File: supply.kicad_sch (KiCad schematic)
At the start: 70 parts, among them J3 Molex_Nano-Fit_1x2_SMD_105430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, Q2 SSM3J332R, Q3 SSM3J332R, Q4 BCM857BS-7-F, Q5 BCM857BS-7-F, Q6 SSM3J332R, Q7 PJE138K, Q8 PJE138K, Q9 SSM3J332R, U1 TPS56C230, U2 TPS56C230

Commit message: [#53804] Clean SD&NVMe sch; Change NVMe to x4; Update 3V3 power sch
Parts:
- removed C11: C_1u_0402, antmicro-footprints:C_0402_1005Metric, symbol antmicroCapacitors0402:C_1u_0402
- removed C13, C9: C_100n_0402, antmicro-footprints:C_0402_1005Metric, symbol antmicroCapacitors0402:C_100n_0402
- removed C14, C16, C18, C20: C_22u_16V_0603, antmicro-footprints:C_0603_1608Metric, symbol antmicroCapacitors0603:C_22u_16V_0603
- removed C5, C7: C_22u_25V_0805, antmicro-footprints:C_0805_2012Metric, symbol antmicroCapacitorsmisc:C_22u_25V_0805
- removed D7: ESD9X5.0ST5G, antmicro-footprints:SOD-923, symbol antmicroTVSDiodes:ESD9X5.0ST5G
- removed L2: L_1u8_14A_Coilcraft-XAL6030, antmicro-footprints:L_Coilcraft-XAL6030, symbol antmicroFixedInductors:L_1u8_14A_Coilcraft-XAL6030
- removed R16: R_220k_0402, antmicro-footprints:R_0402_1005Metric, symbol antmicroResistors0402:R_220k_0402
- removed R17, R20: R_10k_0402, antmicro-footprints:R_0402_1005Metric, symbol antmicroResistors0402:R_10k_0402
- removed R18: R_0R_0402, antmicro-footprints:R_0402_1005Metric, symbol antmicroResistors0402:R_0R_0402
- removed R23: R_90k9_0402, antmicro-footprints:R_0402_1005Metric, symbol antmicroResistors0402:R_90k9_0402
- removed R24: R_20k_0402, antmicro-footprints:R_0402_1005Metric, symbol antmicroResistors0402:R_20k_0402
- removed R26: R_0R_22.4A_0603, antmicro-footprints:R_0603_1608Metric, symbol antmicroResistors0603:R_0R_22.4A_0603
- removed TP4: TP_0.75mm_SMD, antmicro-footprints:TP_SMD_0.75mm, symbol antmicroTestPoints:TP_0.75mm_SMD
- removed U2: TPS56C230, antmicro-footprints:QFN-20-1EP_3x3mm_P0.45mm, symbol antmicroDCDCConverters:TPS56C230
- added C? (x6): C_22u_25V_0805, antmicro-footprints:C_0805_2012Metric, symbol antmicroCapacitorsmisc:C_22u_25V_0805
- added C? (x2): C_100n_0402, scalenode-cm4-baseboard-footprints:C_0402_1005Metric, symbol scalenode-cm4-baseboard:C_100n_0402
- added L? (x2): L_1u_5.5A_SRP3212, antmicro-footprints:L_Bourns-SRP3212A, symbol antmicroFixedInductors:L_1u_5.5A_Bourns-SRP3212A
- added R? (x2): R_10k_0402, scalenode-cm4-baseboard-footprints:R_0402_1005Metric, symbol scalenode-cm4-baseboard:R_10k_0402
- added R? (x2): R_33k2_0402, scalenode-cm4-baseboard-footprints:R_0402_1005Metric, symbol scalenode-cm4-baseboard:R_33k2_0402
- added TP? (x3): TP_1mm_SMD, scalenode-cm4-baseboard-footprints:Testpoint_smd_1mm, symbol scalenode-cm4-baseboard:TP_1mm_SMD
- added U? (x2): AP62301WU-7, antmicro-footprints:TSOT23-6, symbol antmicroDCDCConverters:AP62301_TSOT
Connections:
- net +3V3: now also C?.1, C?.1, L?.2, R?.2, TP?.1
- net GND: now also C?.2, C?.2, C?.2, C?.2, C?.2, C?.2, R?.1, R?.1, U?.1 (GND), U?.1 (GND)
- net VCC: now also C?.1, C?.1, U?.3 (VIN), U?.3 (VIN), U?.5 (EN)
- new net: C?.1, L?.1, U?.2 (SW) (x2)
- new net: R?.1, R?.2, U?.4 (FB) (x2)
- new net: C?.2, U?.6 (BST) (x2)
- new net 3V3_SSD: C?.1, C?.1, L?.2, R?.2, TP?.1
- new net NVMe_EN: TP?.1, U?.5 (EN)
- no-connect marks 2 -> 1
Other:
- note added: "(NFC, CSI, SD, Proximity, UART/USB)"
- note added: "3V3 @ 3A"
- note added: "3V3 DCDC (M.2 NVMe)"
- note added: "3V3 DCDC (Main)"
- note added: "Power requirements: CM: -5V / 2A(RPi) -3.3V&1.8V out / 600m(RPi) DSI/LVDS (DSI84): 1.8V / 150mA WS2812B Strip: 5V / 3.5A/m HDMI: 5V/ 50mA+ CSI: 3V3 / 1.5A? SD card: 3V3 / 100m+? NFC: 3V3/ 350mA+(or 5V partially) proximity: ? 3v3/50mA M.2: 3V3 / 3A UART/USB: -3V3/100mA -1V8/100mA Power Supply: - 1V8 @ 600mA from CM4 - 3V3 @ 3A + 2.2A - 5V @ 6A+"
- note removed: "3V3 @12A"
- note removed: "3V3 DCDC"
- note removed: "Power requirements: CM: -5V / 2A(RPi) -3.3V&1.8V out / 600m(RPi) DSI/LVDS (DSI84): 1.8V / 150mA WS2812B Strip: 5V / 3.5A/m HDMI: 5V/ 50mA+ CSI: 3V3 /? SD card: 3V3 / 100m+? NFC: 3V3/ 350mA+(or 5V partially) proximity: ? 3v3/50mA M.2: 3V3 / 2A? UART/USB: -3V3/60mA -1V8/100mA Power Supply: - 1V8 @ 600mA from CM4 - 3V3 @ 3A+ - 5V @ 6A+"

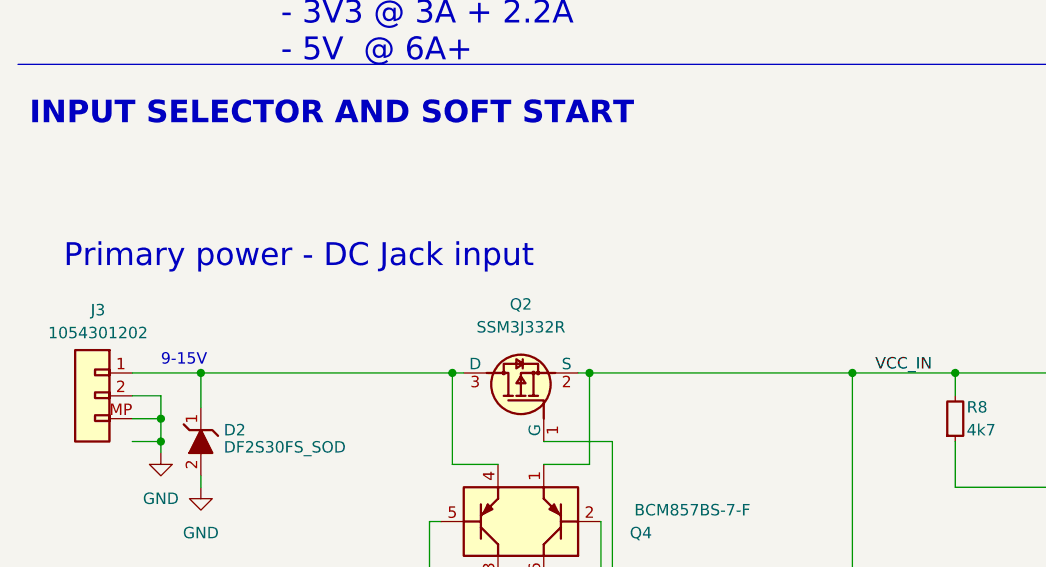
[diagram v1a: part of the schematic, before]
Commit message: [#54231] Clean power supply for LVDS display
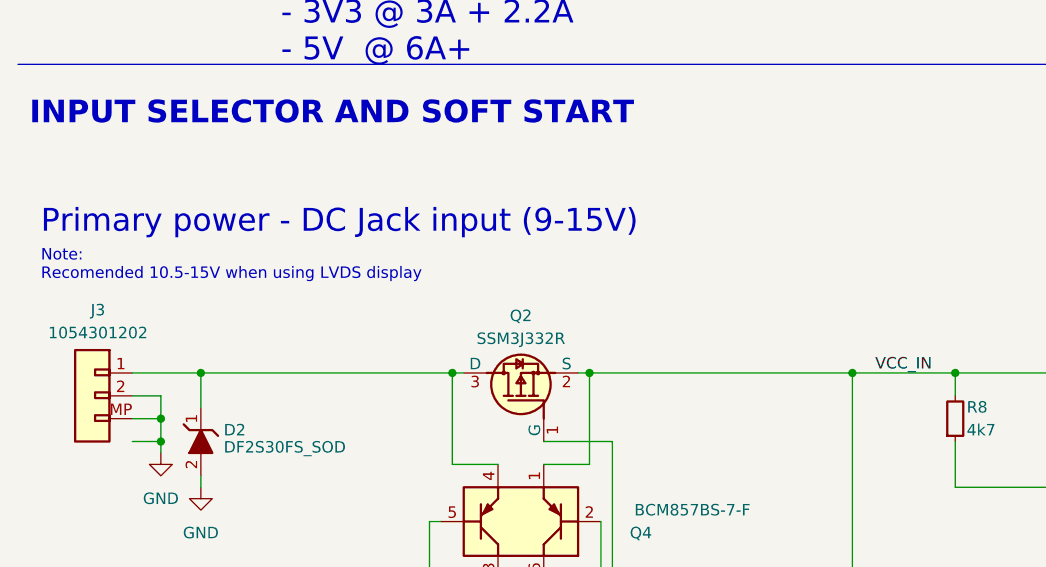
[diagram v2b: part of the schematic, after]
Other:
- note added: "Note: Recomended 10.5-15V when using LVDS display"
- note added: "Primary power - DC Jack input (9-15V)"
- note removed: "9-15V"
- note removed: "Primary power - DC Jack input"
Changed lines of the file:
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@@
     )
   )
+  (text "Note: \nRecomended 10.5-15V when using LVDS display"
+    (at 15.24 118.11 0)
+    (effects (font (size 1.27 1.27)) (justify left bottom))
+  )
   (text " (NFC, CSI, SD, Proximity, UART/USB)" (at 220.98 218.44 0)
     (effects (font (size 1.27 1.27) (thickness 0.254) bold) (justify left bottom))
@@
     (effects (font (size 2.5 2.5) bold) (justify left bottom))
   )
-  (text "9-15V " (at 28.575 127.635 0)
-    (effects (font (size 1.27 1.27)) (justify left bottom))
-  )
   (text "3V3 @ 3A" (at 363.22 176.53 0)
     (effects (font (size 1.27 1.27)) (justify left bottom))
@@
     (effects (font (size 1.27 1.27)) (justify left bottom))
   )
-  (text "Primary power - DC Jack input\n" (at 17.78 116.84 0)
+  (text "Primary power - DC Jack input (9-15V)\n" (at 15.24 113.03 0)
     (effects (font (size 2.54 2.54)) (justify left bottom))
   )
@@
   )
   (symbol (lib_id "antmicroTransistorsFETsMOSFETsSingle:SSM3J332R") (at 71.12 135.89 90) (unit 1)
-    (in_bom yes) (on_board yes) (fields_autoplaced)
-    (property "Reference" "Q2" (id 0) (at 68.58 120.65 90))
-    (property "Value" "SSM3J332R" (id 1) (at 68.58 123.19 90))
+    (in_bom yes) (on_board yes)
+    (property "Reference" "Q2" (id 0) (at 68.58 121.92 90))
+    (property "Value" "SSM3J332R" (id 1) (at 68.58 124.46 90))
     (property "Footprint" "antmicro-footprints:SOT-23-3" (id 2) (at 66.04 130.81 0)
       (effects (font (size 1.524 1.524)) (justify left bottom) hide)

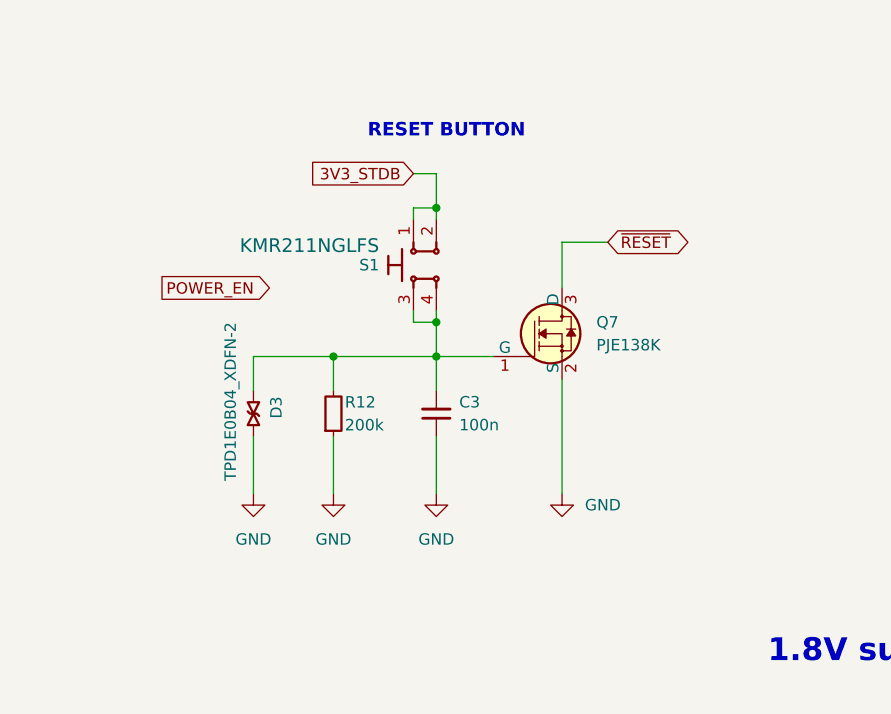
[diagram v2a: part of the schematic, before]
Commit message: [#54447] CM4 connections part 2
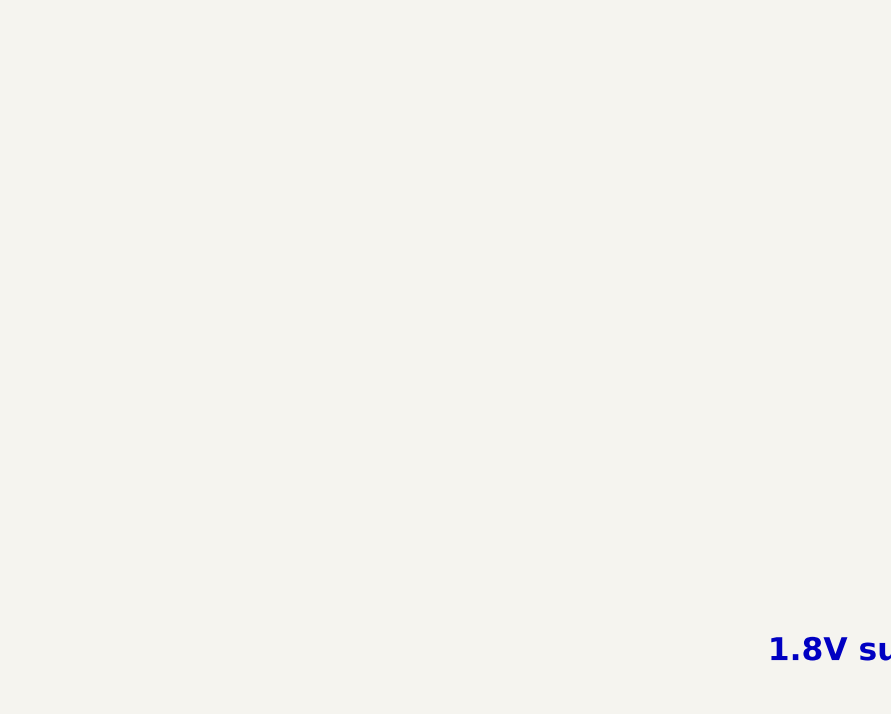
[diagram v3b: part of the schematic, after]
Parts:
- removed C3: C_100n_0402, antmicro-footprints:C_0402_1005Metric, symbol antmicroCapacitors0402:C_100n_0402
- removed D3: TPD1E0B04_XDFN-2, antmicro-footprints:XDFN-2_1x0.60mm, symbol antmicroTVSDiodes:TPD1E0B04_XDFN-2
- removed Q7: PJE138K, antmicro-footprints:SOT-523, symbol antmicroTransistorsFETsMOSFETsSingle:PJE138K
- removed R12: R_200k_0402, antmicro-footprints:R_0402_1005Metric, symbol antmicroResistors0402:R_200k_0402
- removed S1: SW_KMR211NGLFS_SMD, antmicro-footprints:SW_KMR211NGLFS_SMD, symbol antmicroPushbuttonSwitches:SW_KMR211NGLFS_SMD
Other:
- note removed: "RESET BUTTON"

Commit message: [#54474] Complete USB schematics
- merge sch usb&debug
- add USB/4xUART bridge
- add USB-PD managament
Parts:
- C? (x2): footprint scalenode-cm4-baseboard-footprints:C_0402_1005Metric -> antmicro-footprints:C_0402_1005Metric; symbol scalenode-cm4-baseboard:C_100n_0402 -> antmicroCapacitors0402:C_100n_0402
- R? (x2): footprint scalenode-cm4-baseboard-footprints:R_0402_1005Metric -> antmicro-footprints:R_0402_1005Metric; symbol scalenode-cm4-baseboard:R_10k_0402 -> antmicroResistors0402:R_10k_0402
- R? (x2): footprint scalenode-cm4-baseboard-footprints:R_0402_1005Metric -> antmicro-footprints:R_0402_1005Metric; symbol scalenode-cm4-baseboard:R_33k2_0402 -> antmicroResistors0402:R_33k2_0402
- TP? (x3): footprint scalenode-cm4-baseboard-footprints:Testpoint_smd_1mm -> antmicro-footprints:TP_SMD_1mm; symbol scalenode-cm4-baseboard:TP_1mm_SMD -> antmicroTestPoints:TP_1mm_SMD
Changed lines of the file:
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@@
     (pin "2")
   )
-  (symbol (lib_id "scalenode-cm4-baseboard:GND") (at 300.99 242.57 0) (unit 1)
+  (symbol (lib_id "antmicropower:GND") (at 300.99 242.57 0) (unit 1)
     (in_bom yes) (on_board yes) (fields_autoplaced)
     (property "Reference" "#PWR?" (id 0) (at 309.88 245.11 0)
@@
     (pin "1")
   )
-  (symbol (lib_id "scalenode-cm4-baseboard:GND") (at 356.87 242.57 0) (unit 1)
+  (symbol (lib_id "antmicropower:GND") (at 356.87 242.57 0) (unit 1)
     (in_bom yes) (on_board yes) (fields_autoplaced)
     (property "Reference" "#PWR?" (id 0) (at 365.76 245.11 0)
@@
     (pin "2")
   )
-  (symbol (lib_id "scalenode-cm4-baseboard:GND") (at 283.21 242.57 0) (unit 1)
+  (symbol (lib_id "antmicropower:GND") (at 283.21 242.57 0) (unit 1)
     (in_bom yes) (on_board yes) (fields_autoplaced)
     (property "Reference" "#PWR?" (id 0) (at 292.1 245.11 0)
@@
     (pin "2")
   )
-  (symbol (lib_id "scalenode-cm4-baseboard:GND") (at 300.99 196.85 0) (unit 1)
+  (symbol (lib_id "antmicropower:GND") (at 300.99 196.85 0) (unit 1)
     (in_bom yes) (on_board yes) (fields_autoplaced)
     (property "Reference" "#PWR?" (id 0) (at 309.88 199.39 0)
@@
     (pin "1")
   )
-  (symbol (lib_id "scalenode-cm4-baseboard:TP_1mm_SMD") (at 356.87 176.53 90) (unit 1)
+  (symbol (lib_id "antmicroTestPoints:TP_1mm_SMD") (at 356.87 176.53 90) (unit 1)
     (in_bom yes) (on_board yes) (fields_autoplaced)
     (property "Reference" "TP?" (id 0) (at 361.95 173.3549 90)
@@
       (effects (font (size 1.27 1.27) (thickness 0.15)) (justify left bottom) hide)
     )
-    (property "Footprint" "scalenode-cm4-baseboard-footprints:Testpoint_smd_1mm" (id 2) (at 367.03 161.29 0)
+    (property "Footprint" "antmicro-footprints:TP_SMD_1mm" (id 2) (at 367.03 161.29 0)
       (effects (font (size 1.27 1.27) (thickness 0.15)) (justify left bottom) hide)
     )
@@
     (pin "1")
   )
-  (symbol (lib_id "scalenode-cm4-baseboard:R_10k_0402") (at 345.44 195.58 90) (unit 1)
+  (symbol (lib_id "antmicroResistors0402:R_10k_0402") (at 345.44 195.58 90) (unit 1)
     (in_bom yes) (on_board yes)
     (property "Reference" "R?" (id 0) (at 346.71 193.04 90)
@@
       (effects (font (size 1.27 1.27) (thickness 0.15)) (justify left bottom) hide)
     )
-    (property "Footprint" "scalenode-cm4-baseboard-footprints:R_0402_1005Metric" (id 2) (at 360.68 175.26 0)
+    (property "Footprint" "antmicro-footprints:R_0402_1005Metric" (id 2) (at 360.68 175.26 0)
       (effects (font (size 1.27 1.27) (thickness 0.15)) (justify left bottom) hide)
     )
@@
     (pin "2")
   )
-  (symbol (lib_id "scalenode-cm4-baseboard:TP_1mm_SMD") (at 297.18 182.88 90) (unit 1)
+  (symbol (lib_id "antmicroTestPoints:TP_1mm_SMD") (at 297.18 182.88 90) (unit 1)
     (in_bom yes) (on_board yes) (fields_autoplaced)
     (property "Reference" "TP?" (id 0) (at 299.72 179.7049 90)
@@
       (effects (font (size 1.27 1.27) (thickness 0.15)) (justify left bottom) hide)
     )
-    (property "Footprint" "scalenode-cm4-baseboard-footprints:Testpoint_smd_1mm" (id 2) (at 307.34 167.64 0)
+    (property "Footprint" "antmicro-footprints:TP_SMD_1mm" (id 2) (at 307.34 167.64 0)
       (effects (font (size 1.27 1.27) (thickness 0.15)) (justify left bottom) hide)
     )
@@
     (pin "1")
   )
-  (symbol (lib_id "scalenode-cm4-baseboard:GND") (at 345.44 242.57 0) (unit 1)
+  (symbol (lib_id "antmicropower:GND") (at 345.44 242.57 0) (unit 1)
     (in_bom yes) (on_board yes) (fields_autoplaced)
     (property "Reference" "#PWR?" (id 0) (at 354.33 245.11 0)
@@
     (pin "1")
   )
-  (symbol (lib_id "scalenode-cm4-baseboard:TP_1mm_SMD") (at 356.87 222.25 90) (unit 1)
+  (symbol (lib_id "antmicroTestPoints:TP_1mm_SMD") (at 356.87 222.25 90) (unit 1)
     (in_bom yes) (on_board yes) (fields_autoplaced)
     (property "Reference" "TP?" (id 0) (at 361.95 219.0749 90)
@@
       (effects (font (size 1.27 1.27) (thickness 0.15)) (justify left bottom) hide)
     )
-    (property "Footprint" "scalenode-cm4-baseboard-footprints:Testpoint_smd_1mm" (id 2) (at 367.03 207.01 0)
+    (property "Footprint" "antmicro-footprints:TP_SMD_1mm" (id 2) (at 367.03 207.01 0)
       (effects (font (size 1.27 1.27) (thickness 0.15)) (justify left bottom) hide)
     )
@@
     (pin "1")
   )
-  (symbol (lib_id "scalenode-cm4-baseboard:GND") (at 283.21 196.85 0) (unit 1)
+  (symbol (lib_id "antmicropower:GND") (at 283.21 196.85 0) (unit 1)
     (in_bom yes) (on_board yes) (fields_autoplaced)
     (property "Reference" "#PWR?" (id 0) (at 292.1 199.39 0)
@@
     (pin "6")
   )
-  (symbol (lib_id "scalenode-cm4-baseboard:C_100n_0402") (at 330.2 182.88 180) (unit 1)
+  (symbol (lib_id "antmicroCapacitors0402:C_100n_0402") (at 330.2 182.88 180) (unit 1)
     (in_bom yes) (on_board yes)
     (property "Reference" "C?" (id 0) (at 327.66 180.34 0)
@@
       (effects (font (size 1.27 1.27) (thickness 0.15)) (justify left bottom) hide)
     )
-    (property "Footprint" "scalenode-cm4-baseboard-footprints:C_0402_1005Metric" (id 2) (at 309.88 170.18 0)
+    (property "Footprint" "antmicro-footprints:C_0402_1005Metric" (id 2) (at 309.88 170.18 0)
       (effects (font (size 1.27 1.27) (thickness 0.15)) (justify left bottom) hide)
     )
@@
     (pin "2")
   )
-  (symbol (lib_id "scalenode-cm4-baseboard:GND") (at 367.03 242.57 0) (unit 1)
+  (symbol (lib_id "antmicropower:GND") (at 367.03 242.57 0) (unit 1)
     (in_bom yes) (on_board yes) (fields_autoplaced)
     (property "Reference" "#PWR?" (id 0) (at 375.92 245.11 0)
@@
     (pin "2")
   )
-  (symbol (lib_id "scalenode-cm4-baseboard:R_33k2_0402") (at 345.44 185.42 90) (unit 1)
+  (symbol (lib_id "antmicroResistors0402:R_33k2_0402") (at 345.44 185.42 90) (unit 1)
     (in_bom yes) (on_board yes)
     (property "Reference" "R?" (id 0) (at 346.71 182.88 90)
@@
       (effects (font (size 1.27 1.27) (thickness 0.15)) (justify left bottom) hide)
     )
-    (property "Footprint" "scalenode-cm4-baseboard-footprints:R_0402_1005Metric" (id 2) (at 360.68 165.1 0)
+    (property "Footprint" "antmicro-footprints:R_0402_1005Metric" (id 2) (at 360.68 165.1 0)
       (effects (font (size 1.27 1.27) (thickness 0.15)) (justify left bottom) hide)
     )
@@
     (pin "2")
   )
-  (symbol (lib_id "scalenode-cm4-baseboard:R_10k_0402") (at 345.44 241.3 90) (unit 1)
+  (symbol (lib_id "antmicroResistors0402:R_10k_0402") (at 345.44 241.3 90) (unit 1)
     (in_bom yes) (on_board yes)
     (property "Reference" "R?" (id 0) (at 346.71 238.76 90)
@@
       (effects (font (size 1.27 1.27) (thickness 0.15)) (justify left bottom) hide)
     )
-    (property "Footprint" "scalenode-cm4-baseboard-footprints:R_0402_1005Metric" (id 2) (at 360.68 220.98 0)
+    (property "Footprint" "antmicro-footprints:R_0402_1005Metric" (id 2) (at 360.68 220.98 0)
       (effects (font (size 1.27 1.27) (thickness 0.15)) (justify left bottom) hide)
     )
@@
     (pin "2")
   )
-  (symbol (lib_id "scalenode-cm4-baseboard:GND") (at 356.87 196.85 0) (unit 1)
+  (symbol (lib_id "antmicropower:GND") (at 356.87 196.85 0) (unit 1)
     (in_bom yes) (on_board yes) (fields_autoplaced)
     (property "Reference" "#PWR?" (id 0) (at 365.76 199.39 0)
@@
     (pin "2")
   )
-  (symbol (lib_id "scalenode-cm4-baseboard:GND") (at 345.44 196.85 0) (unit 1)
+  (symbol (lib_id "antmicropower:GND") (at 345.44 196.85 0) (unit 1)
     (in_bom yes) (on_board yes) (fields_autoplaced)
     (property "Reference" "#PWR?" (id 0) (at 354.33 199.39 0)
@@
     (pin "1")
   )
-  (symbol (lib_id "scalenode-cm4-baseboard:C_100n_0402") (at 330.2 228.6 180) (unit 1)
+  (symbol (lib_id "antmicroCapacitors0402:C_100n_0402") (at 330.2 228.6 180) (unit 1)
     (in_bom yes) (on_board yes)
     (property "Reference" "C?" (id 0) (at 327.66 226.06 0)
@@
       (effects (font (size 1.27 1.27) (thickness 0.15)) (justify left bottom) hide)
     )
-    (property "Footprint" "scalenode-cm4-baseboard-footprints:C_0402_1005Metric" (id 2) (at 309.88 215.9 0)
+    (property "Footprint" "antmicro-footprints:C_0402_1005Metric" (id 2) (at 309.88 215.9 0)
       (effects (font (size 1.27 1.27) (thickness 0.15)) (justify left bottom) hide)
     )
@@
     (pin "2")
   )
-  (symbol (lib_id "scalenode-cm4-baseboard:R_33k2_0402") (at 345.44 231.14 90) (unit 1)
+  (symbol (lib_id "antmicroResistors0402:R_33k2_0402") (at 345.44 231.14 90) (unit 1)
     (in_bom yes) (on_board yes)
     (property "Reference" "R?" (id 0) (at 346.71 228.6 90)
@@
       (effects (font (size 1.27 1.27) (thickness 0.15)) (justify left bottom) hide)
     )
-    (property "Footprint" "scalenode-cm4-baseboard-footprints:R_0402_1005Metric" (id 2) (at 360.68 210.82 0)
+    (property "Footprint" "antmicro-footprints:R_0402_1005Metric" (id 2) (at 360.68 210.82 0)
       (effects (font (size 1.27 1.27) (thickness 0.15)) (justify left bottom) hide)
     )
@@
     (pin "1")
   )
-  (symbol (lib_id "scalenode-cm4-baseboard:GND") (at 367.03 196.85 0) (unit 1)
+  (symbol (lib_id "antmicropower:GND") (at 367.03 196.85 0) (unit 1)
     (in_bom yes) (on_board yes) (fields_autoplaced)
     (property "Reference" "#PWR?" (id 0) (at 375.92 199.39 0)
